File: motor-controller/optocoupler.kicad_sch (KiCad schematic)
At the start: 5 parts, among them U1 MCT6

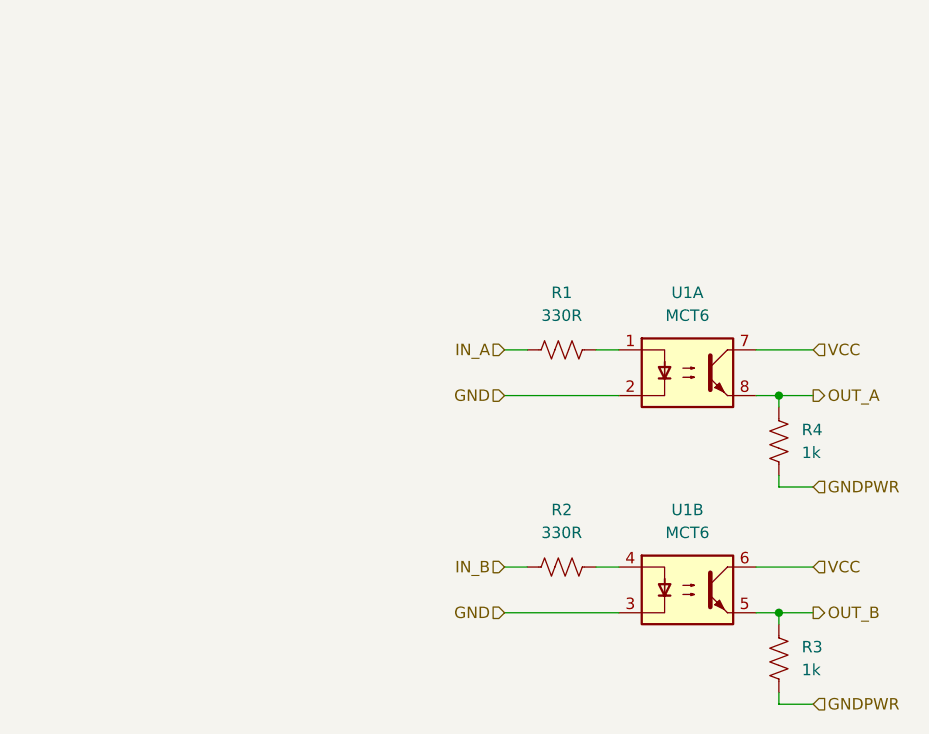
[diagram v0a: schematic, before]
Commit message: Finish H-Bridge schematic
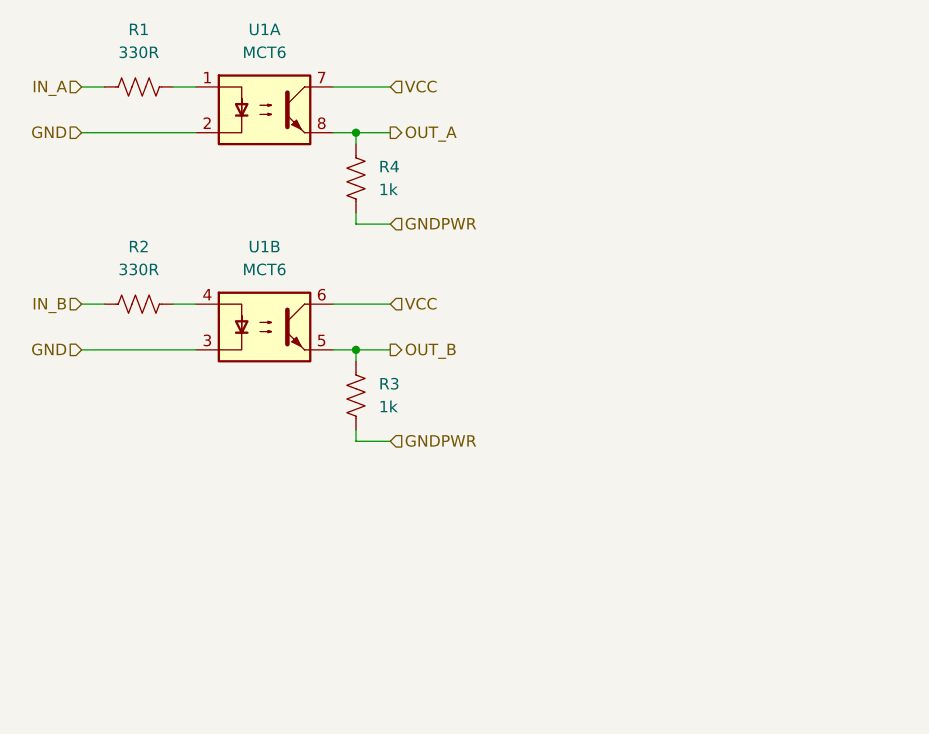
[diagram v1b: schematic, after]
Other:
- moved on the sheet: R1, R2, R3, R4, U1A, U1B

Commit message: Fix some ERC issues
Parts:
- renumbered R1 to R13, R4 to R14, R2 to R15, R3 to R16, U1 to U2
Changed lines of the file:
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@@
 		(dnp no)
 		(fields_autoplaced yes)
-		(property "Reference" "U1"
+		(property "Reference" "U2"
 			(at 105.41 43.18 0)
 			(effects
@@
 				)
 				(path "/3cf627b4-179f-4b19-ad57-a5207e12b14c/b71eba93-a5ac-44ab-8657-fb36dfe25929"
-					(reference "U1")
+					(reference "U2")
 					(unit 1)
 				)
@@
 		(on_board yes)
 		(dnp no)
-		(property "Reference" "U1"
+		(property "Reference" "U2"
 			(at 105.41 67.31 0)
 			(effects
@@
 				)
 				(path "/3cf627b4-179f-4b19-ad57-a5207e12b14c/b71eba93-a5ac-44ab-8657-fb36dfe25929"
-					(reference "U1")
+					(reference "U2")
 					(unit 2)
 				)
@@
 		(dnp no)
 		(fields_autoplaced yes)
-		(property "Reference" "R4"
+		(property "Reference" "R14"
 			(at 118.11 58.4199 0)
 			(effects
@@
 			(project "motor-controller"
 				(path "/3cf627b4-179f-4b19-ad57-a5207e12b14c/8df6f006-2f8a-45b2-b2f5-cd2a57657185"
-					(reference "R7")
-					(unit 1)
-				)
-				(path "/3cf627b4-179f-4b19-ad57-a5207e12b14c/b71eba93-a5ac-44ab-8657-fb36dfe25929"
-					(reference "R4")
+					(reference "R18")
+					(unit 1)
+				)
+				(path "/3cf627b4-179f-4b19-ad57-a5207e12b14c/b71eba93-a5ac-44ab-8657-fb36dfe25929"
+					(reference "R14")
 					(unit 1)
 				)
@@
 		(dnp no)
 		(fields_autoplaced yes)
-		(property "Reference" "R3"
+		(property "Reference" "R16"
 			(at 118.11 82.5499 0)
 			(effects
@@
 			(project "motor-controller"
 				(path "/3cf627b4-179f-4b19-ad57-a5207e12b14c/8df6f006-2f8a-45b2-b2f5-cd2a57657185"
-					(reference "R8")
-					(unit 1)
-				)
-				(path "/3cf627b4-179f-4b19-ad57-a5207e12b14c/b71eba93-a5ac-44ab-8657-fb36dfe25929"
-					(reference "R3")
+					(reference "R20")
+					(unit 1)
+				)
+				(path "/3cf627b4-179f-4b19-ad57-a5207e12b14c/b71eba93-a5ac-44ab-8657-fb36dfe25929"
+					(reference "R16")
 					(unit 1)
 				)
@@
 		(dnp no)
 		(fields_autoplaced yes)
-		(property "Reference" "R1"
+		(property "Reference" "R13"
 			(at 91.44 43.18 90)
 			(effects
@@
 			(project "motor-controller"
 				(path "/3cf627b4-179f-4b19-ad57-a5207e12b14c/8df6f006-2f8a-45b2-b2f5-cd2a57657185"
-					(reference "R5")
-					(unit 1)
-				)
-				(path "/3cf627b4-179f-4b19-ad57-a5207e12b14c/b71eba93-a5ac-44ab-8657-fb36dfe25929"
-					(reference "R1")
+					(reference "R17")
+					(unit 1)
+				)
+				(path "/3cf627b4-179f-4b19-ad57-a5207e12b14c/b71eba93-a5ac-44ab-8657-fb36dfe25929"
+					(reference "R13")
 					(unit 1)
 				)
@@
 		(dnp no)
 		(fields_autoplaced yes)
-		(property "Reference" "R2"
+		(property "Reference" "R15"
 			(at 91.44 67.31 90)
 			(effects
@@
 			(project "motor-controller"
 				(path "/3cf627b4-179f-4b19-ad57-a5207e12b14c/8df6f006-2f8a-45b2-b2f5-cd2a57657185"
-					(reference "R6")
-					(unit 1)
-				)
-				(path "/3cf627b4-179f-4b19-ad57-a5207e12b14c/b71eba93-a5ac-44ab-8657-fb36dfe25929"
-					(reference "R2")
-					(unit 1)
-				)
+					(reference "R19")
+					(unit 1)
+				)
+				(path "/3cf627b4-179f-4b19-ad57-a5207e12b14c/b71eba93-a5ac-44ab-8657-fb36dfe25929"
+					(reference "R15")
+					(unit 1)
+				)

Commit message: Finish layout
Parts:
- R14, R16: value 1k -> 10k
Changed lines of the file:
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@@
 			)
 		)
-		(property "Value" "1k"
+		(property "Value" "10k"
 			(at 118.11 60.9599 0)
 			(effects
@@
 			)
 		)
-		(property "Value" "1k"
+		(property "Value" "10k"
 			(at 118.11 85.0899 0)
 			(effects
